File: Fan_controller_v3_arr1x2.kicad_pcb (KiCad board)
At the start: 4 copper layers, 50 x 50 mm, 0 parts

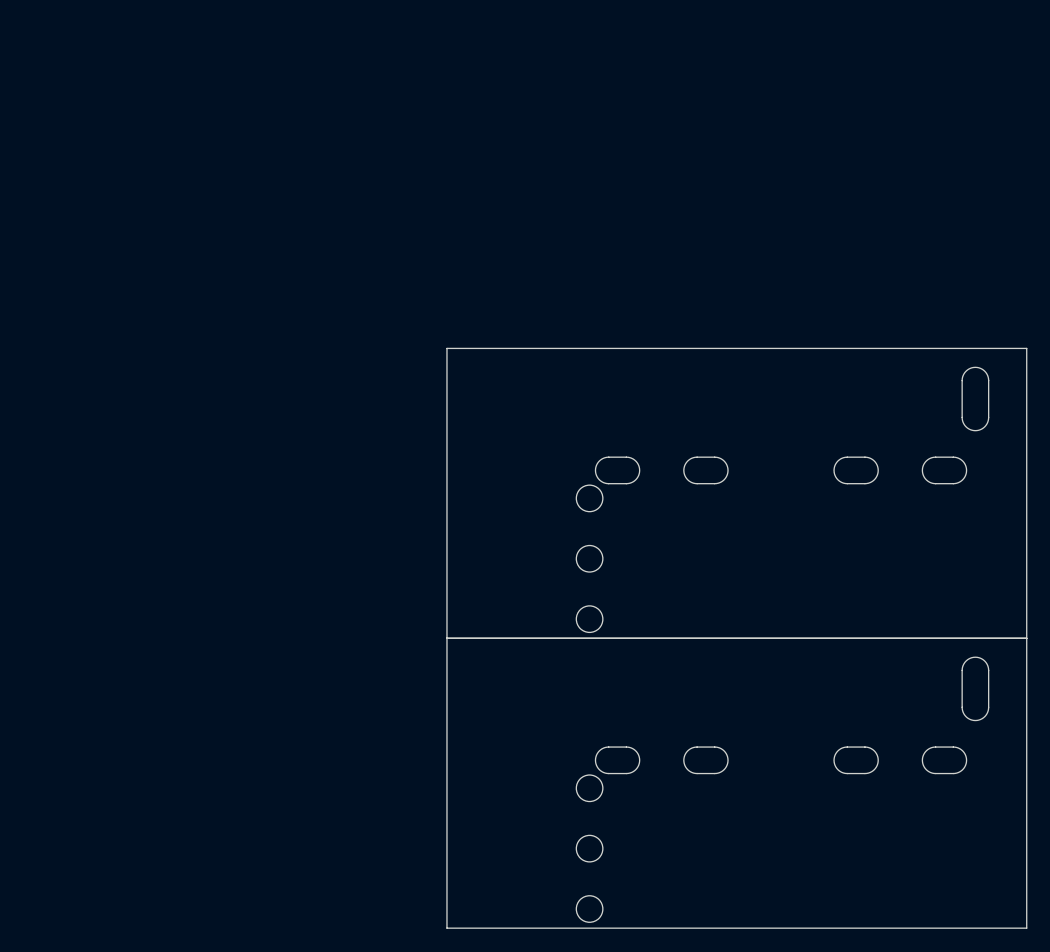
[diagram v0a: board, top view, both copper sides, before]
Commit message: Сформирован перечень элементов, 3D-модель, исправлены ошибки, реализована панелизация платы.
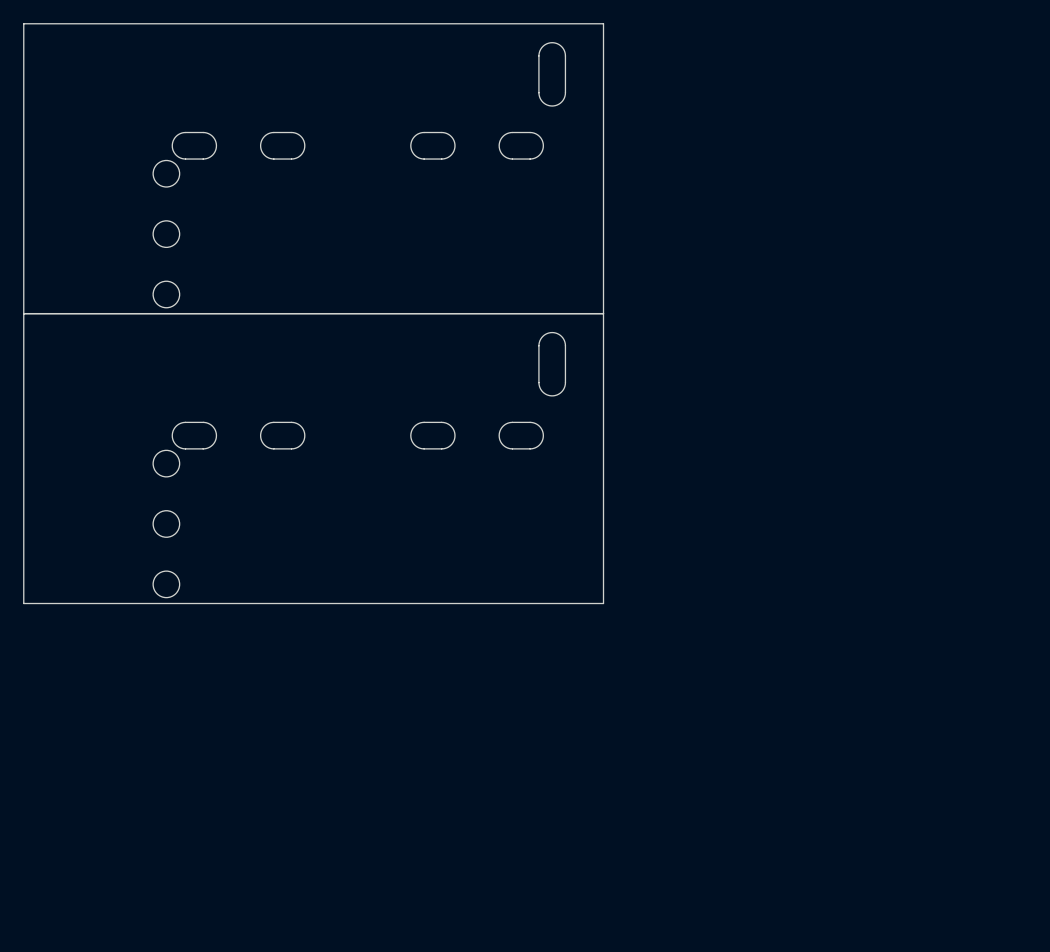
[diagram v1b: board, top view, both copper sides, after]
